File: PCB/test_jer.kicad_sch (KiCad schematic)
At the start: 14 parts, among them J1 AudioJack2, J2 AudioJack2, Q1 BSS138, U1 Pico, U2 MAX481E

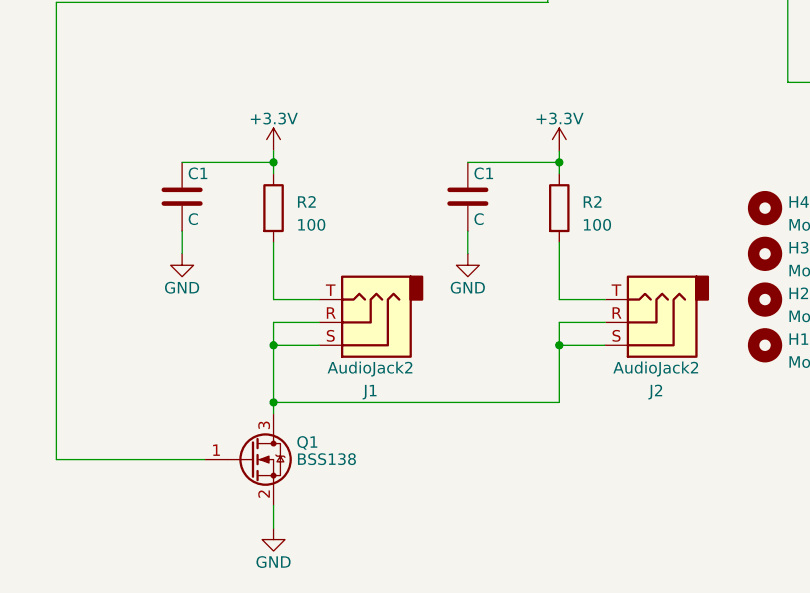
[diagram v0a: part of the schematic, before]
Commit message: Fixed switched source and drain on PMOS
On 12V common source amp for level shifter in subcircuit
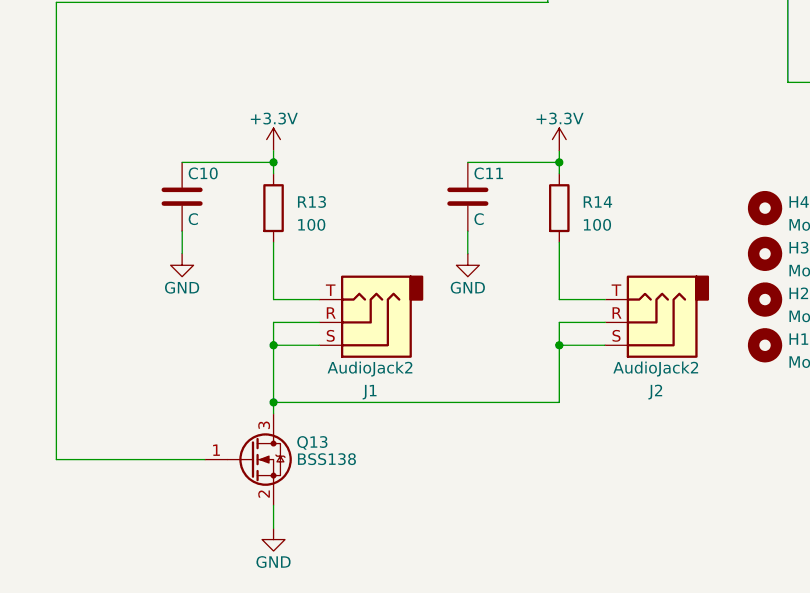
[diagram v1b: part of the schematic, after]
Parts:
- renumbered C1 to C10, C1 to C11, Q1 to Q13, R2 to R13, R2 to R14
